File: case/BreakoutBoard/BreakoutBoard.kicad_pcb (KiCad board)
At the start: 2 copper layers, 130 x 60 mm, 18 parts

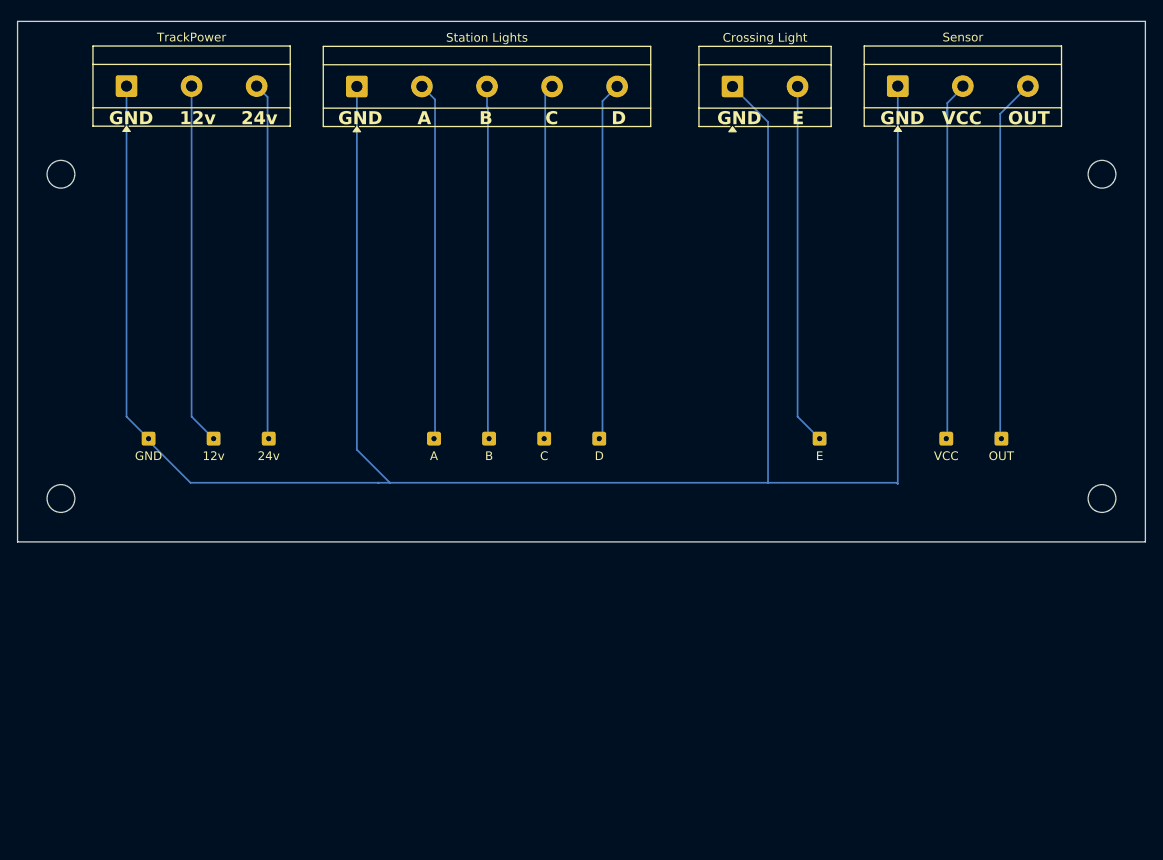
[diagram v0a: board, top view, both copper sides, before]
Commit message: add a breakout board and connector stuff
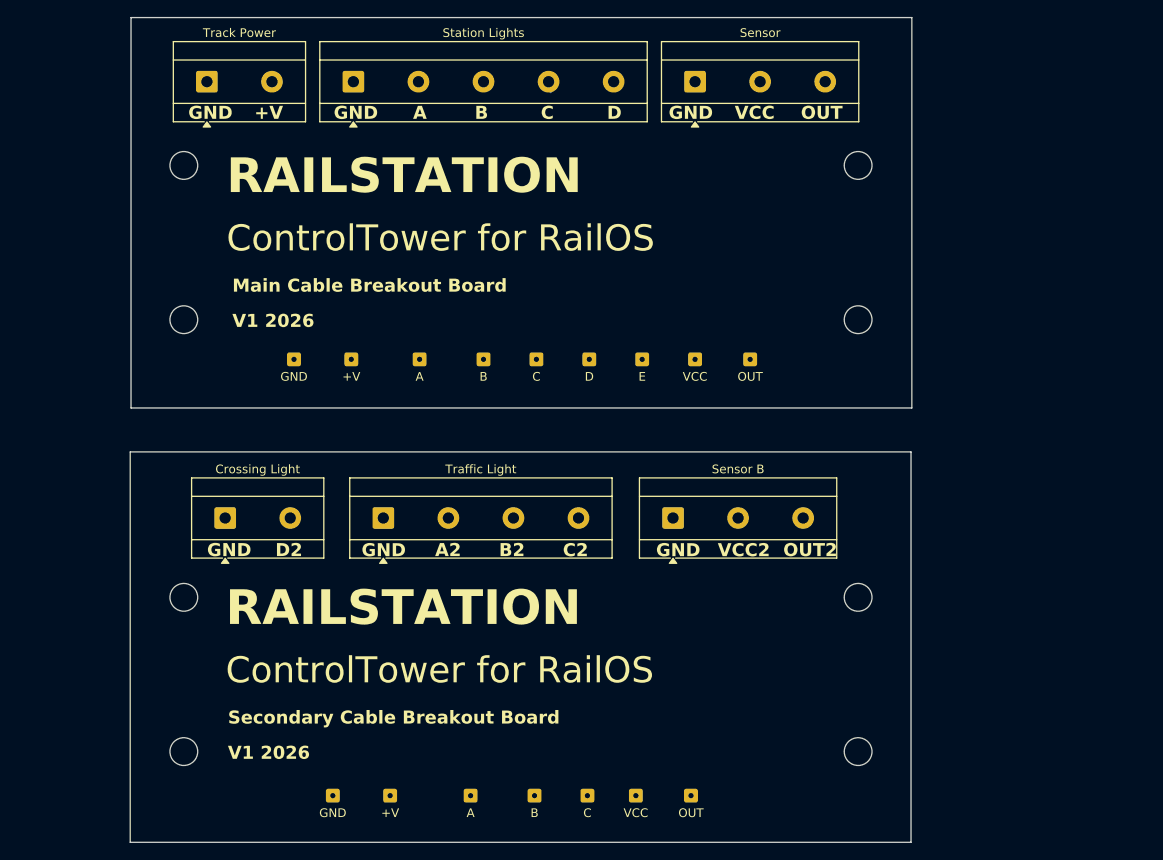
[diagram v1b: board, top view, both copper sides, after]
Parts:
- removed 24v: GND, Connector_Wire:SolderWire-0.1sqmm_1x01_D0.4mm_OD1mm
- removed TrackPower: Track Power, TerminalBlock_MetzConnect:TerminalBlock_MetzConnect_Type171_RT13703HBWC_1x03_P7.50mm_Horizontal
- added +V: GND, Connector_Wire:SolderWire-0.1sqmm_1x01_D0.4mm_OD1mm, F.Cu at (60.9, 107.2)
- added A: GND, Connector_Wire:SolderWire-0.1sqmm_1x01_D0.4mm_OD1mm, F.Cu at (70.1, 107.2)
- added B: GND, Connector_Wire:SolderWire-0.1sqmm_1x01_D0.4mm_OD1mm, F.Cu at (77.5, 107.2)
- added B.R.: MountingHole_3.2mm_M3, MountingHole:MountingHole_3.2mm_M3, F.Cu at (114.8, 102.1)
- added BottomLeft: MountingHole_3.2mm_M3, MountingHole:MountingHole_3.2mm_M3, F.Cu at (37.1, 102.1)
- added C: GND, Connector_Wire:SolderWire-0.1sqmm_1x01_D0.4mm_OD1mm, F.Cu at (83.6, 107.2)
- added GND: GND, Connector_Wire:SolderWire-0.1sqmm_1x01_D0.4mm_OD1mm, F.Cu at (54.3, 107.2)
- added OUT: GND, Connector_Wire:SolderWire-0.1sqmm_1x01_D0.4mm_OD1mm, F.Cu at (95.5, 107.2)
- added Sensor B: Sensor, TerminalBlock_MetzConnect:TerminalBlock_MetzConnect_Type171_RT13703HBWC_1x03_P7.50mm_Horizontal, F.Cu at (93.5, 75.2)
- added TopLeft: MountingHole_3.2mm_M3, MountingHole:MountingHole_3.2mm_M3, F.Cu at (37.1, 84.3)
- added TopRight: MountingHole_3.2mm_M3, MountingHole:MountingHole_3.2mm_M3, F.Cu at (114.8, 84.3)
- added Track Power: Crossing Light, TerminalBlock_MetzConnect:TerminalBlock_MetzConnect_Type171_RT13702HBWC_1x02_P7.50mm_Horizontal, F.Cu at (39.7, 24.9)
- added Traffic Light: TerminalBlock_MetzConnect_Type171_RT13704HBWC_1x04_P7.50mm_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, TerminalBlock_MetzConnect:TerminalBlock_MetzConnect_Type171_RT13704HBWC_1x04_P7.50mm_Horizontal, F.Cu at (60.1, 75.2)
- added VCC: GND, Connector_Wire:SolderWire-0.1sqmm_1x01_D0.4mm_OD1mm, F.Cu at (89.2, 107.2)
- moved Crossing Light 76.8 mm to (41.9, 75.2)
- moved B.R. 34.9 mm to (114.8, 52.3)
- moved OUT 30.4 mm to (102.4, 56.9)
- moved VCC 30.4 mm to (96.0, 56.9)
- moved TopRight 28.0 mm to (114.8, 34.5)
- moved BottomLeft 25.0 mm to (37.1, 52.3)
- moved Sensor 23.4 mm to (96.0, 24.9)
- moved E 22.4 mm to (89.9, 56.9)
- moved GND 19.1 mm to (49.8, 56.9)
- moved +V 18.3 mm to (56.4, 56.9)
- moved TopLeft 14.2 mm to (37.1, 34.5)
- moved A 9.29 mm to (64.3, 56.9)
- moved D 9.22 mm to (83.8, 56.9)
- moved C 9.19 mm to (77.7, 56.9)
- moved B 9.17 mm to (71.6, 56.9)
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- renumbered 12v to +V
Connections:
- Crossing Light pad 1: GND -> GND2
- Crossing Light pad 2: E -> D2
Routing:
- net GND: track 272.4 -> 0.00 mm
- net OUT: track 43.2 -> 0.19 mm
- net VCC: track 42.4 -> 0.17 mm
- net 12v: track 41.7 -> 0.00 mm
- net E: track 41.7 -> 0.00 mm
- net D: track 41.5 -> 0.00 mm
- net 24v: track 41.2 -> 0.00 mm
- net A: track 41.3 -> 0.17 mm
- net B: track 40.7 -> 0.00 mm
- net C: track 41.0 -> 1.12 mm
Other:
- board size 130 x 60 mm -> 90.1 x 95.1 mm
- board text added: "+V"
- board text added: "A2"
- board text added: "B2"
- board text added: "C2"
- board text added: "ControlTower for RailOS"
- board text added: "D2"
- board text added: "Main Cable Breakout Board"
- board text added: "OUT2"
- board text added: "RAILSTATION"
- board text added: "Secondary Cable Breakout Board"
- board text added: "V1 2026"
- board text added: "VCC2"
- board text removed: "12v"
- board text removed: "24v"
- board text removed: "E"

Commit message: rest of it
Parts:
- removed E: GND, Connector_Wire:SolderWire-0.1sqmm_1x01_D0.4mm_OD1mm
- moved Crossing Light 0.51 mm to (41.9, 74.7)
- moved Sensor B 0.51 mm to (93.5, 74.7)
- moved Traffic Light 0.51 mm to (60.1, 74.7)
- renumbered OUT to OUT2
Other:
- board text removed: "D2"

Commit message: updates moving toward start of manufacture
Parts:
- added ?: , , F.Cu at (60.5, 107.2)
- added Control Switch: Crossing Light, TerminalBlock_MetzConnect:TerminalBlock_MetzConnect_Type171_RT13702HBWC_1x02_P7.50mm_Horizontal, F.Cu at (35.7, 74.7)
- Traffic Signal: renamed from Traffic Light
- moved Crossing Light 10.8 mm to (52.6, 74.7)
- moved Traffic Signal 9.13 mm to (69.2, 74.7)
- moved Sensor B 7.62 mm to (101.1, 74.7)
- moved CRSD 5.68 mm to (66.5, 107.2)
- moved +5V 3.30 mm to (92.7, 56.9)
- moved STNB 3.30 mm to (74.9, 56.9)
- moved STND 3.30 mm to (87.1, 56.9)
- moved +V 3.30 mm to (59.7, 56.9)
- moved OUT 3.30 mm to (99.1, 56.9)
- moved STNA 3.30 mm to (67.6, 56.9)
- moved STNC 3.30 mm to (81.0, 56.9)
- moved +5V 3.05 mm to (92.2, 107.2)
- moved OUT 3.05 mm to (98.6, 107.2)
- moved SIGA 3.05 mm to (73.2, 107.2)
- moved SIGC 3.05 mm to (86.7, 107.2)
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- renumbered VCC to +5V, +V to CRSD, OUT2 to OUT, A to SIGA, B to SIGB, C to SIGC, A to STNA, B to STNB, C to STNC, D to STND
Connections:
- CRSD pad 1: V2 -> D2
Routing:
- net GND: track 0.00 -> 134.8 mm
- net GND2: track 0.00 -> 110.4 mm
- net OUT2: track 0.19 -> 40.6 mm
- net CTL: track 0.00 -> 39.7 mm
- net VCC2: track 0.17 -> 39.5 mm
- net 12v: track 0.00 -> 37.2 mm
- net OUT: track 0.19 -> 37.1 mm
- net VCC: track 0.17 -> 36.6 mm
- net D2: track 0.00 -> 35.2 mm
- net C2: track 0.00 -> 34.6 mm
- net B2: track 0.00 -> 34.1 mm
- net A2: track 0.17 -> 34.1 mm
- net A: track 0.17 -> 33.6 mm
- net B: track 0.00 -> 33.4 mm
- net C: track 1.12 -> 33.9 mm
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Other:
- board text added: "+5V"
- board text added: "+5v"
- board text added: "CRSD"
- board text added: "CTL"
- board text added: "SIGA"
- board text added: "SIGB"
- board text added: "SIGC"
- board text added: "STNA"
- board text added: "STNB"
- board text added: "STNC"
- board text added: "STND"
- board text removed: "A"
- board text removed: "A2"
- board text removed: "B"
- board text removed: "B2"
- board text removed: "C"
- board text removed: "C2"
- board text removed: "D"
- board text removed: "OUT2"
- board text removed: "VCC"
- board text removed: "VCC2"

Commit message: let's update!
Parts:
- removed the +5V at (92.2, 107.2)
- removed the +5V at (92.7, 56.9)
- removed +V, STNA, STNB, STNC, STND: GND, Connector_Wire:SolderWire-0.1sqmm_1x01_D0.4mm_OD1mm
- removed the B.R. at (114.8, 102.1)
- removed the B.R. at (114.8, 52.3)
- removed the BottomLeft at (37.1, 102.1)
- removed the BottomLeft at (37.1, 52.3)
- removed the GND at (52.6, 56.9)
- removed the GND at (53.8, 107.2)
- removed the OUT at (99.1, 56.9)
- removed the OUT at (98.6, 107.2)
- removed Sensor: Sensor, TerminalBlock_MetzConnect:TerminalBlock_MetzConnect_Type171_RT13703HBWC_1x03_P7.50mm_Horizontal
- removed Station Lights: Station Lights, TerminalBlock_MetzConnect:TerminalBlock_MetzConnect_Type171_RT13705HBWC_1x05_P7.50mm_Horizontal
- removed the TopLeft at (37.1, 34.5)
- removed the TopLeft at (37.1, 84.3)
- removed the TopRight at (114.8, 84.3)
- removed the TopRight at (114.8, 34.5)
- removed Track Power: Crossing Light, TerminalBlock_MetzConnect:TerminalBlock_MetzConnect_Type171_RT13702HBWC_1x02_P7.50mm_Horizontal
- added +5V: GND, Connector_Wire:SolderWire-0.1sqmm_1x01_D0.4mm_OD1mm, F.Cu at (89.2, 62.2)
- added B.R.: MountingHole_3.2mm_M3, MountingHole:MountingHole_3.2mm_M3, F.Cu at (111.8, 57.1)
- added BottomLeft: MountingHole_3.2mm_M3, MountingHole:MountingHole_3.2mm_M3, F.Cu at (34.0, 57.1)
- added GND: GND, Connector_Wire:SolderWire-0.1sqmm_1x01_D0.4mm_OD1mm, F.Cu at (50.8, 62.2)
- added OUT: GND, Connector_Wire:SolderWire-0.1sqmm_1x01_D0.4mm_OD1mm, F.Cu at (95.5, 62.2)
- added TopLeft: MountingHole_3.2mm_M3, MountingHole:MountingHole_3.2mm_M3, F.Cu at (34.0, 39.3)
- added TopRight: MountingHole_3.2mm_M3, MountingHole:MountingHole_3.2mm_M3, F.Cu at (111.8, 39.3)
- moved ? 45.1 mm to (57.5, 62.2)
- moved CRSD 45.1 mm to (63.5, 62.2)
- moved Control Switch 45.1 mm to (32.6, 29.7)
- moved Crossing Light 45.1 mm to (49.6, 29.7)
- moved SIGA 45.1 mm to (70.1, 62.2)
- moved SIGB 45.1 mm to (77.2, 62.2)
- moved SIGC 45.1 mm to (83.6, 62.2)
- moved Sensor B 45.1 mm to (98.0, 29.7)
- moved Traffic Signal 45.1 mm to (66.2, 29.7)
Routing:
- net GND: track 134.8 -> 0.00 mm
- net 12v: track 37.2 -> 0.00 mm
- net OUT: track 37.1 -> 0.00 mm
- net VCC: track 36.6 -> 0.00 mm
- net C: track 33.9 -> 0.00 mm
- net A: track 33.6 -> 0.00 mm
- net B: track 33.4 -> 0.00 mm
- net D: track 32.2 -> 0.00 mm
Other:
- board size 90.1 x 95.1 mm -> 90 x 45 mm
- board text removed: "+5V"
- board text removed: "+V"
- board text removed: "Main Cable Breakout Board"
- board text removed: "STNA"
- board text removed: "STNB"
- board text removed: "STNC"
- board text removed: "STND"
